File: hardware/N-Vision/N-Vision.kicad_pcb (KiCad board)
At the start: 2 copper layers, 3 parts, among them J1 547220164, J2 555600168

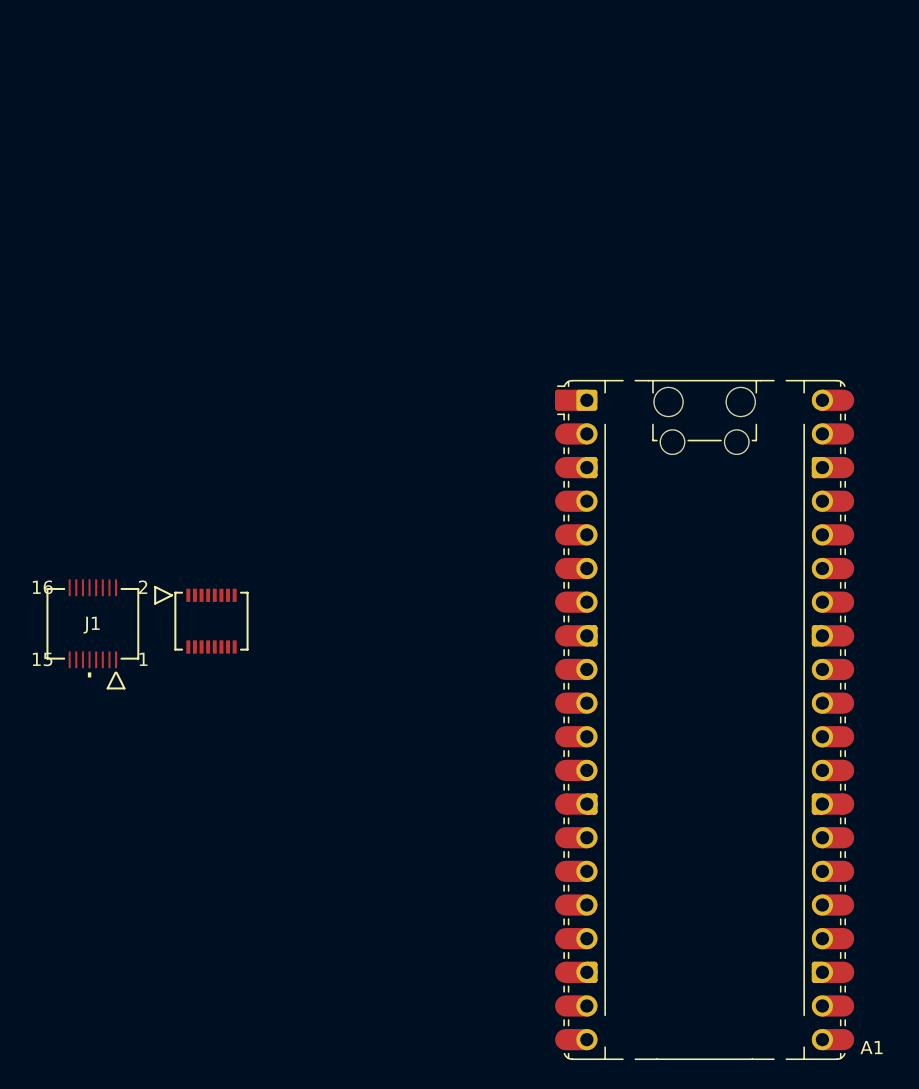
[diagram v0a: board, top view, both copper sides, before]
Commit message: Update footprints (one needed to be reversed)
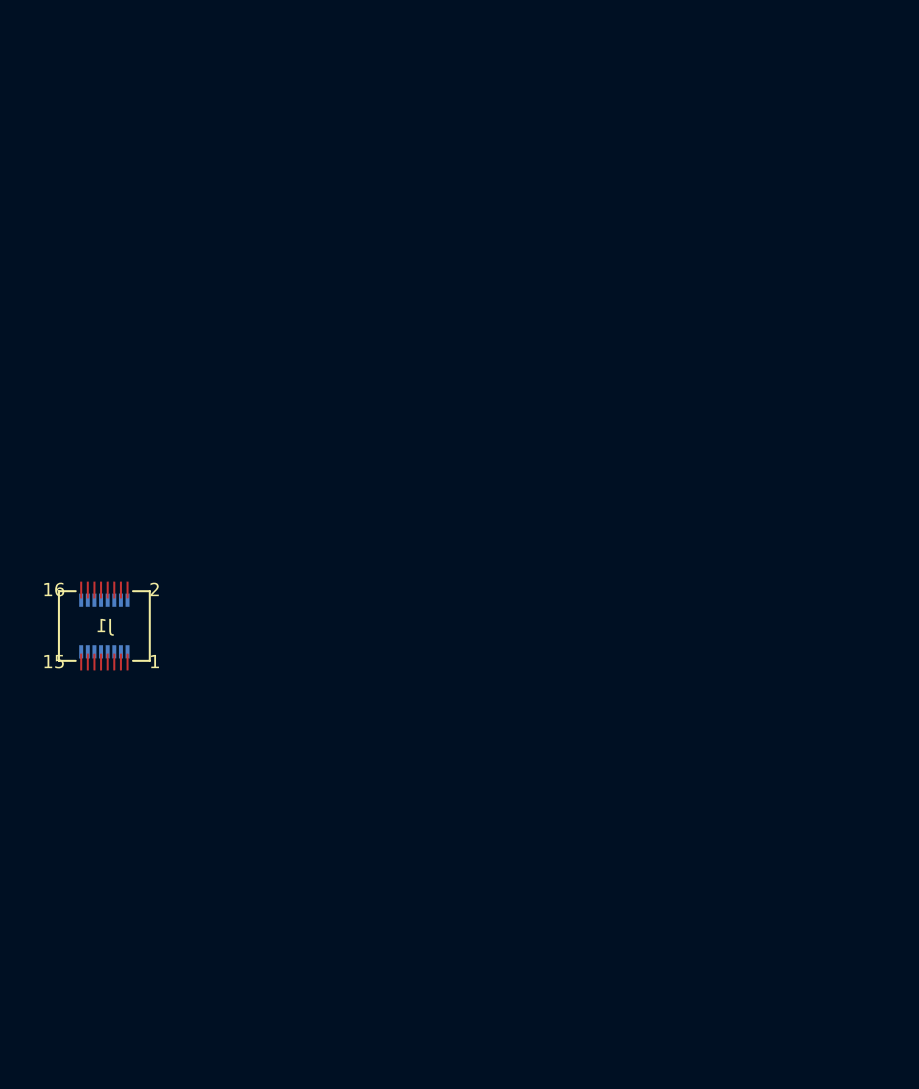
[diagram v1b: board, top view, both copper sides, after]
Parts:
- removed A1: RaspberryPi_Pico, Module:RaspberryPi_Pico_Common_Unspecified
- J2: footprint footprints:CON_555600168 -> footprints:CONN_55560-0168_MOL; moved to B.Cu
- moved J2 8.09 mm to (130.0, 84.0)
- moved J1 0.88 mm to (130.0, 84.0)
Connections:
- J1 pad 1: unconnected-(J1-Pad1) -> GND
- J1 pad 10: unconnected-(J1-Pad10) -> /LCDDa6
- J1 pad 11: unconnected-(J1-Pad11) -> /LCDDa3
- J1 pad 12: unconnected-(J1-Pad12) -> /LCDDa5
- J1 pad 13: unconnected-(J1-Pad13) -> /LCDDa4
- J1 pad 16: unconnected-(J1-Pad16) -> GND
- J1 pad 3: unconnected-(J1-Pad3) -> /LCDM
- J1 pad 4: unconnected-(J1-Pad4) -> /LCDDISPClk
- J1 pad 5: unconnected-(J1-Pad5) -> /LCDDa0
- J1 pad 7: unconnected-(J1-Pad7) -> /LCDDa1
- J1 pad 8: unconnected-(J1-Pad8) -> /LCDDa7
- J1 pad 9: unconnected-(J1-Pad9) -> /LCDDa2
- J2 pad 1: unconnected-(J2-Pad1) -> GND
- J2 pad 10: unconnected-(J2-Pad10) -> /LCDDa6
- J2 pad 11: unconnected-(J2-Pad11) -> /LCDDa3
- J2 pad 12: unconnected-(J2-Pad12) -> /LCDDa5
- J2 pad 13: unconnected-(J2-Pad13) -> /LCDDa4
- J2 pad 16: unconnected-(J2-Pad16) -> GND
- J2 pad 3: unconnected-(J2-Pad3) -> /LCDM
- J2 pad 4: unconnected-(J2-Pad4) -> /LCDDISPClk
- J2 pad 5: unconnected-(J2-Pad5) -> /LCDDa0
- J2 pad 7: unconnected-(J2-Pad7) -> /LCDDa1
- J2 pad 8: unconnected-(J2-Pad8) -> /LCDDa7
- J2 pad 9: unconnected-(J2-Pad9) -> /LCDDa2

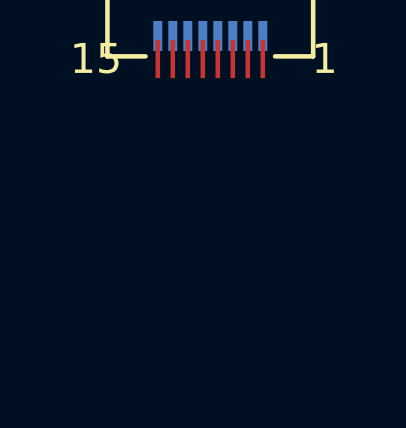
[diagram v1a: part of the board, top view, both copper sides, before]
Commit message: Update BOM, add FPC connector.
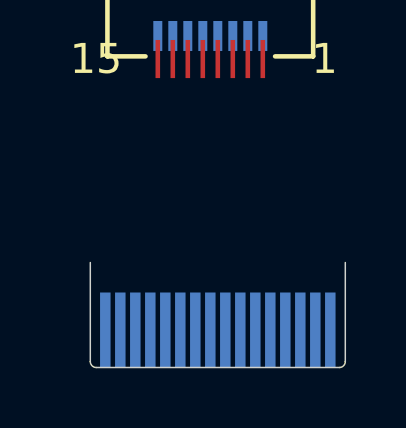
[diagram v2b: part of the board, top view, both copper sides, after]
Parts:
- added J3: FPC/FFC, footprints:FPC-16P-0.5mm, B.Cu at (126.5, 95.8)
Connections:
- J1 pad 14: unconnected-(J1-Unused-Pad14) -> /Unused 3
- J1 pad 15: unconnected-(J1-Unused-Pad15) -> /Unused 4
- J1 pad 2: unconnected-(J1-Unused-Pad2) -> /Unused 1
- J1 pad 6: unconnected-(J1-Unused-Pad6) -> /Unused 2
- J2 pad 14: unconnected-(J2-Unused-Pad14) -> /Unused 3
- J2 pad 15: unconnected-(J2-Unused-Pad15) -> /Unused 4
- J2 pad 2: unconnected-(J2-Unused-Pad2) -> /Unused 1
- J2 pad 6: unconnected-(J2-Unused-Pad6) -> /Unused 2
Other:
- board outline added: 8.5 x 3.5 mm

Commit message: Update center.
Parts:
- moved J1 41.5 mm to (130.0, 42.5)
- moved J2 41.5 mm to (130.0, 42.5)
- moved J3 23.5 mm to (130.0, 72.5)
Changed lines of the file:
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@@
 	(footprint "footprints:CONN_54722-0164_MOL"
 		(layer "F.Cu")
-		(at 130 84)
+		(at 130 42.5)
 		(tags "547220164 ")
 		(property "Reference" "J1"
@@
 	(footprint "footprints:FPC-16P-0.5mm"
 		(layer "B.Cu")
-		(at 126.5 95.75)
+		(at 130 72.5)
 		(property "Reference" "J3"
 			(at 0 -2.25 180)
@@
 		(sheetname "/")
 		(sheetfile "N-Vision.kicad_sch")
-		(units
-			(unit
-				(name "A")
-				(pins "2" "6" "14" "15" "3" "4" "5" "7" "9" "11" "13" "12" "10" "8" "1"
-					"16"
-				)
-			)
-		)
 		(attr smd)
 		(duplicate_pad_numbers_are_jumpers no)
 		(fp_line
-			(start -0.5 -2.25)
-			(end -0.5 1.05)
+			(start -4.25 -3.5)
+			(end -4.25 -0.2)
 			(stroke
 				(width 0.05)
@@
 		)
 		(fp_line
-			(start -0.3 1.25)
-			(end 7.8 1.25)
+			(start -4.05 0)
+			(end 4.05 0)
 			(stroke
 				(width 0.05)
@@
 		)
 		(fp_line
-			(start 8 -2.25)
-			(end 8 1.05)
+			(start 4.25 -3.5)
+			(end 4.25 -0.2)
 			(stroke
 				(width 0.05)
@@
 		)
 		(fp_arc
-			(start -0.3 1.25)
-			(mid -0.441421 1.191421)
-			(end -0.5 1.05)
+			(start -4.05 0)
+			(mid -4.191421 -0.058579)
+			(end -4.25 -0.2)
 			(stroke
 				(width 0.05)
@@
 		)
 		(fp_arc
-			(start 8 1.05)
-			(mid 7.941421 1.191421)
-			(end 7.8 1.25)
+			(start 4.25 -0.2)
+			(mid 4.191421 -0.058579)
+			(end 4.05 0)
 			(stroke
 				(width 0.05)
@@
 		)
 		(fp_line
-			(start -0.5 -2.25)
-			(end -0.5 1.05)
+			(start -4.25 -3.5)
+			(end -4.25 -0.2)
 			(stroke
 				(width 0.05)
@@
 		)
 		(fp_line
-			(start -0.5 -2.25)
-			(end 8 -2.25)
+			(start -4.25 -3.5)
+			(end 4.25 -3.5)
 			(stroke
 				(width 0.05)
@@
 		)
 		(fp_line
-			(start -0.3 1.25)
-			(end 7.8 1.25)
+			(start -4.05 0)
+			(end 4.05 0)
 			(stroke
 				(width 0.05)
@@
 		)
 		(fp_line
-			(start 8 -2.25)
-			(end 8 1.05)
+			(start 4.25 -3.5)
+			(end 4.25 -0.2)
 			(stroke
 				(width 0.05)
@@
 		)
 		(fp_arc
-			(start -0.3 1.25)
-			(mid -0.441421 1.191421)
-			(end -0.5 1.05)
+			(start -4.05 0)
+			(mid -4.191421 -0.058579)
+			(end -4.25 -0.2)
 			(stroke
 				(width 0.05)
@@
 		)
 		(fp_arc
-			(start 8 1.05)
-			(mid 7.941421 1.191421)
-			(end 7.8 1.25)
+			(start 4.25 -0.2)
+			(mid 4.191421 -0.058579)
+			(end 4.05 0)
 			(stroke
 				(width 0.05)
@@
 		)
 		(pad "1" smd rect
-			(at 0 0 270)
+			(at -3.75 -1.25 270)
 			(size 2.5 0.35)
 			(layers "B.Cu" "B.Mask" "B.Paste")
@@
 		)
 		(pad "2" smd rect
-			(at 0.5 0 270)
+			(at -3.25 -1.25 270)
 			(size 2.5 0.35)
 			(layers "B.Cu" "B.Mask" "B.Paste")
@@
 		)
 		(pad "3" smd rect
-			(at 1 0 270)
+			(at -2.75 -1.25 270)
 			(size 2.5 0.35)
 			(layers "B.Cu" "B.Mask" "B.Paste")
@@
 		)
 		(pad "4" smd rect
-			(at 1.5 0 270)
+			(at -2.25 -1.25 270)
 			(size 2.5 0.35)
 			(layers "B.Cu" "B.Mask" "B.Paste")
@@
 		)
 		(pad "5" smd rect
-			(at 2 0 270)
+			(at -1.75 -1.25 270)
 			(size 2.5 0.35)
 			(layers "B.Cu" "B.Mask" "B.Paste")
@@
 		)
 		(pad "6" smd rect
-			(at 2.5 0 270)
+			(at -1.25 -1.25 270)
 			(size 2.5 0.35)
 			(layers "B.Cu" "B.Mask" "B.Paste")
@@
 		)
 		(pad "7" smd rect
-			(at 3 0 270)
+			(at -0.75 -1.25 270)
 			(size 2.5 0.35)
 			(layers "B.Cu" "B.Mask" "B.Paste")
@@
 		)
 		(pad "8" smd rect
-			(at 3.5 0 270)
+			(at -0.25 -1.25 270)
 			(size 2.5 0.35)
 			(layers "B.Cu" "B.Mask" "B.Paste")
@@
 		)
 		(pad "9" smd rect
-			(at 4 0 270)
+			(at 0.25 -1.25 270)
 			(size 2.5 0.35)
 			(layers "B.Cu" "B.Mask" "B.Paste")
@@
 		)
 		(pad "10" smd rect
-			(at 4.5 0 270)
+			(at 0.75 -1.25 270)
 			(size 2.5 0.35)
 			(layers "B.Cu" "B.Mask" "B.Paste")
@@
 		)
 		(pad "11" smd rect
-			(at 5 0 270)
+			(at 1.25 -1.25 270)
 			(size 2.5 0.35)
 			(layers "B.Cu" "B.Mask" "B.Paste")
@@
 		)
 		(pad "12" smd rect
-			(at 5.5 0 270)
+			(at 1.75 -1.25 270)
 			(size 2.5 0.35)
 			(layers "B.Cu" "B.Mask" "B.Paste")
@@
 		)
 		(pad "13" smd rect
-			(at 6 0 270)
+			(at 2.25 -1.25 270)
 			(size 2.5 0.35)
 			(layers "B.Cu" "B.Mask" "B.Paste")
@@
 		)
 		(pad "14" smd rect
-			(at 6.5 0 270)
+			(at 2.75 -1.25 270)
 			(size 2.5 0.35)
 			(layers "B.Cu" "B.Mask" "B.Paste")
@@
 		)
 		(pad "15" smd rect
-			(at 7 0 270)
+			(at 3.25 -1.25 270)
 			(size 2.5 0.35)
 			(layers "B.Cu" "B.Mask" "B.Paste")
@@
 		)
 		(pad "16" smd rect
-			(at 7.5 0 270)
+			(at 3.75 -1.25 270)
 			(size 2.5 0.35)
 			(layers "B.Cu" "B.Mask" "B.Paste")
@@
 	(footprint "footprints:CONN_55560-0168_MOL"
 		(layer "B.Cu")
-		(at 130 84)
+		(at 130 42.5)
 		(tags "555600168 ")
 		(property "Reference" "J2"
